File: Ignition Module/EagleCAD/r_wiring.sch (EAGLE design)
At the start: 51 parts, among them T1 BC848, T2 BC848, T3 BC848, T4 ZXTP2041F, T5 BUB323Z

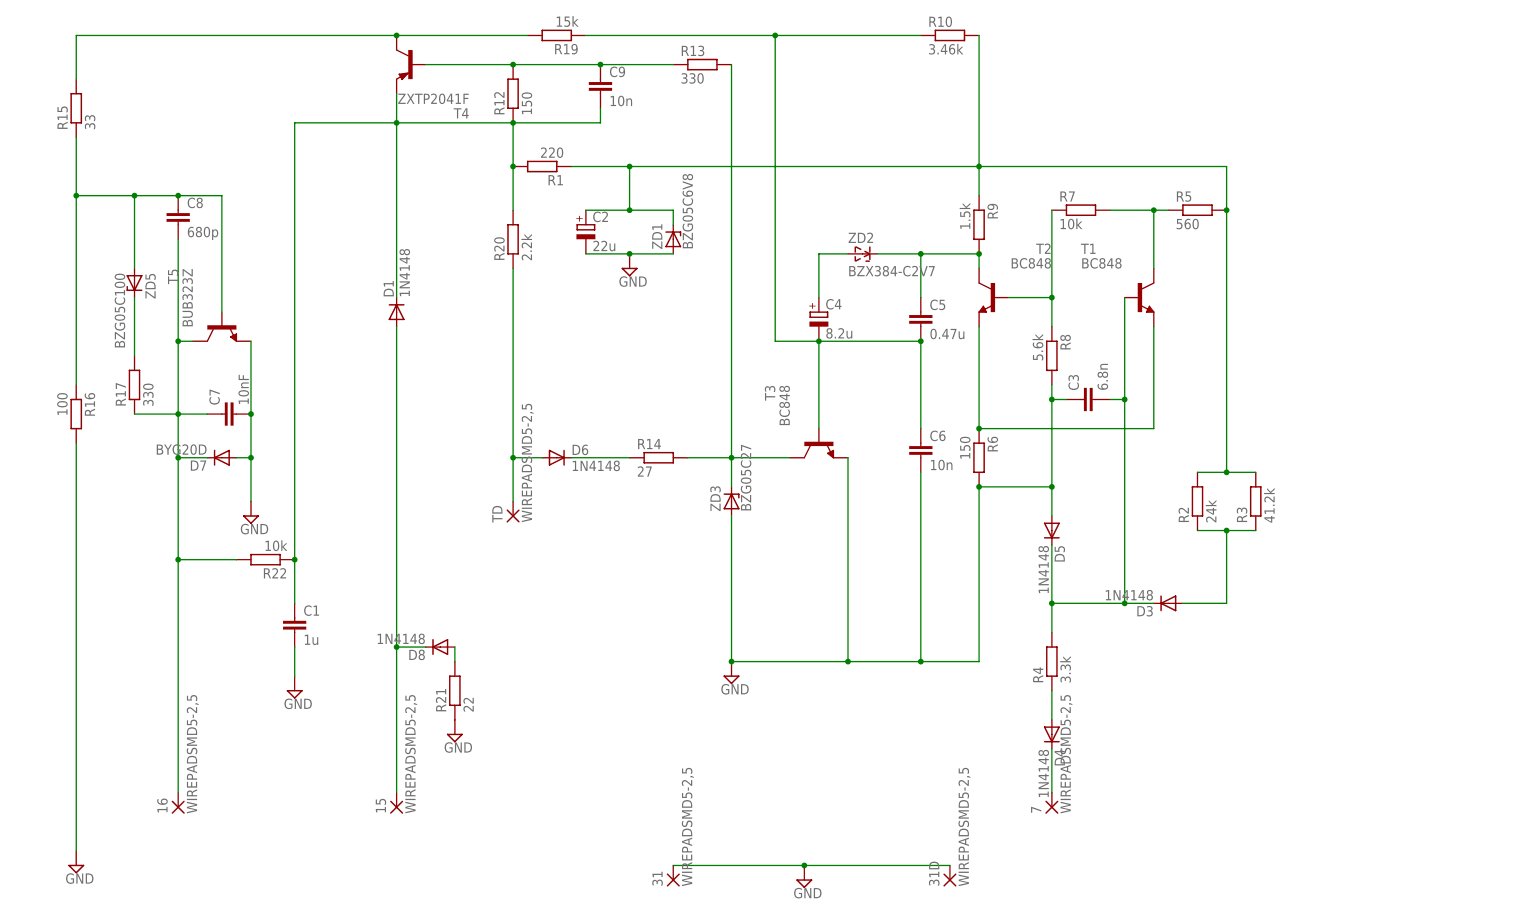
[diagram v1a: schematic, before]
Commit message: Circuit and board updates
Updated circuit with functional layout and annotations. Revised and
added component ratings. Added BOM. Updated board layout. Updates
provided by djenka018 of http://forum.w116.org
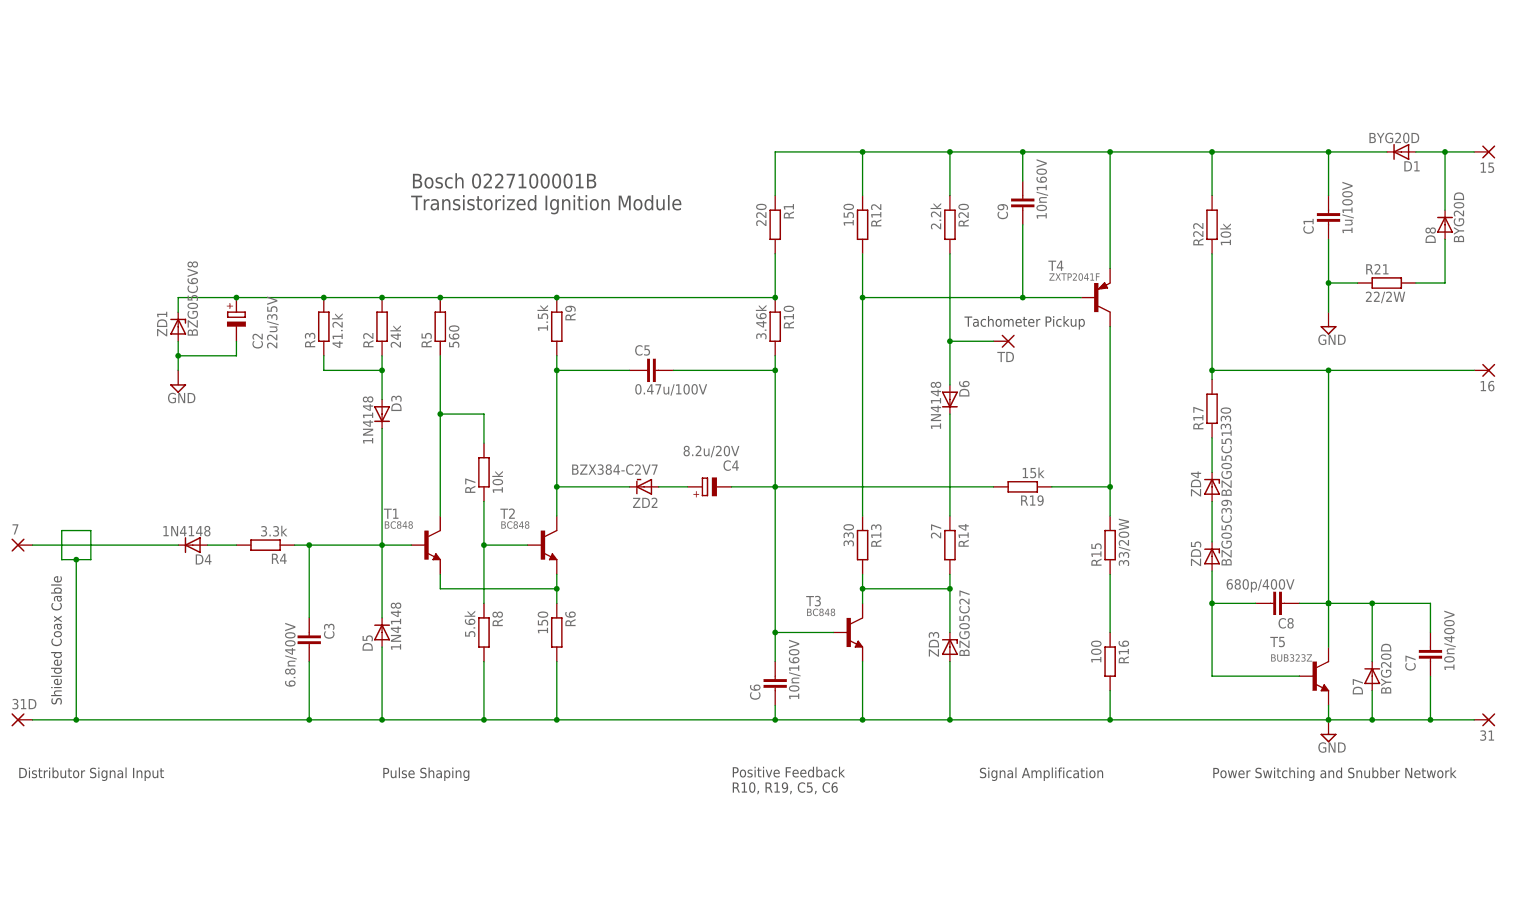
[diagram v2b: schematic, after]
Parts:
- added ZD4: BZG05C51, diode:ZENER-DIODESMB
- C1: value 1u -> 1u/100V
- C2: value 22u -> 22u/35V
- C3: value 6.8n -> 6.8n/400V
- C4: value 8.2u -> 8.2u/20V
- C5: value 0.47u -> 0.47u/100V
- C6, C9: value 10n -> 10n/160V
- C7: value 10nF -> 10n/400V
- C8: value 680p -> 680p/400V
- D1, D8: value 1N4148 -> BYG20D
- R15: value 33 -> 33/20W; WATTAGE >=20W -> (none)
- R21: value 22 -> 22/2W
- ZD5: value BZG05C100 -> BZG05C39
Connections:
- removed net N$1: C8.1, R15.1, R16.1, T5.B, ZD5.A
- removed net N$2 (its old number): R15.2, R19.2, T4.C
- removed net N$20 (its old number): D6.A, R20.1, TD.P
- removed net N$28: R17.2, ZD5.C
- removed net N$29: 16.P, C7.1, C8.2, D7.C, R17.1, R22.2, T5.C
- removed net N$31: C2.+, R1.1, R10.2, R2.2, R3.2, R5.2, R9.1, ZD1.C
- new net N$11: C5.2, R9.2, T2.C, ZD2.C
- new net N$13: R15.2, R19.1, T4.C
- new net N$14: C1.1, C9.1, D1.C, R1.1, R12.1, R20.1, R22.2, T4.E
- new net N$15: D6.A, R20.2, TD.P
- new net N$23: ZD4.A, ZD5.C
- new net N$25: C8.1, T5.B, ZD5.A
- new net N$3: D4.A, R4.2
- new net N$8: C2.+, R1.2, R10.1, R2.2, R3.2, R5.2, R9.1, ZD1.C
- net N$12: now also C4.-, C5.1, C6.1, R10.2, R19.2, T3.B; no longer D4.A, R4.1
- net N$16: now also C9.2, R12.2, R13.1, T4.B; no longer C4.-, C5.2, C6.1, R10.1, R19.1, T3.B
- net N$18: now also R15.1, R16.1; no longer C5.1, R9.2, T2.C, ZD2.C
- net N$21: now also R17.1, ZD4.C; no longer C1.1, C9.2, D1.C, R1.2, R12.1, R20.2, R22.1, T4.E
- net N$22: now also 16.P, C7.1, C8.2, D7.C, R17.2, R22.1, T5.C; no longer C9.1, R12.2, R13.1, T4.B
- net N$4: now also R4.1; no longer R4.2
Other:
- note added: "Bosch 0227100001B Transistorized Ignition Module"
- note added: "Distributor Signal Input"
- note added: "Positive Feedback R10, R19, C5, C6"
- note added: "Power Switching and Snubber Network"
- note added: "Pulse Shaping"
- note added: "Shielded Coax Cable"
- note added: "Signal Amplification"
- note added: "Tachometer Pickup"
- moved on the sheet: 15, 16, 31, 31D, 7, C1, C2, C3, C4, C5, C6, C7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
